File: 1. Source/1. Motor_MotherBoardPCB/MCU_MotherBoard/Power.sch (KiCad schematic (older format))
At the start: 3 parts, among them J10 Connector_JST_01x02, J9 Connector_JST_01x02, U20 LM7805CT

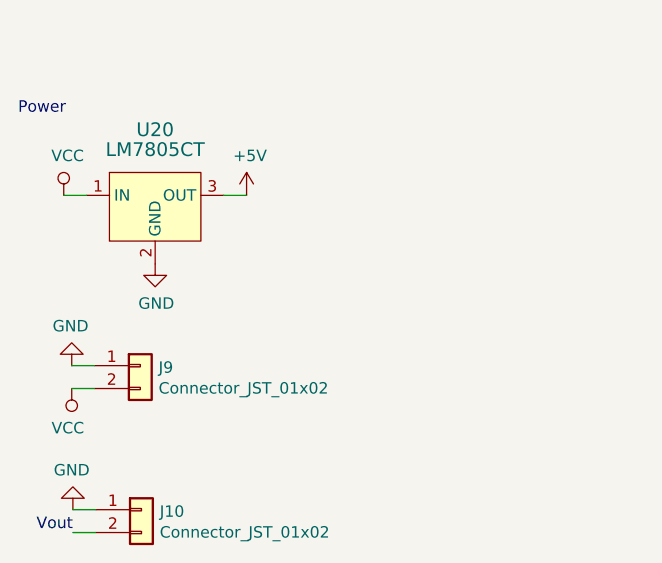
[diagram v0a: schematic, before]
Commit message: Schematic finished
- change cap`s footprint to smd type
- artwork should be done.
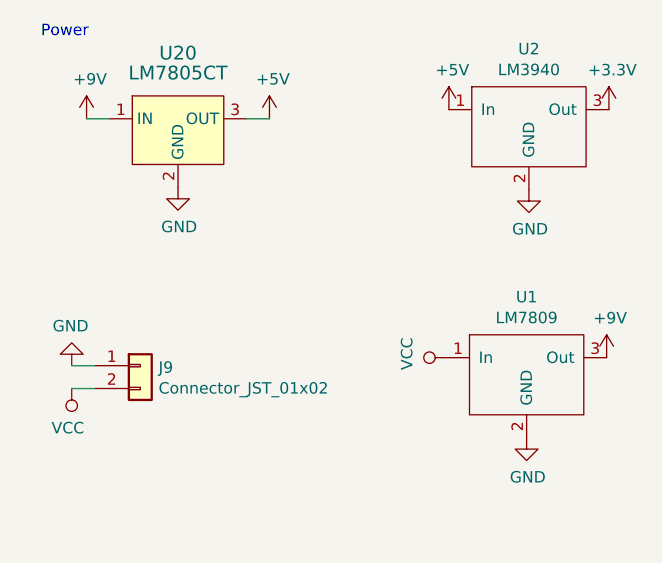
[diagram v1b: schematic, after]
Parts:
- removed J10: Connector_JST_01x02, Connectors_JST:JST_XH_S02B-XH-A_02x2.50mm_Angled, symbol BC_Connectors:Connector_JST_01x02
- added U1: LM7809, digikey-footprints:TO-220-3, symbol BC_IC_components:LM7809
- added U2: LM3940, digikey-footprints:TO-220-3, symbol BC_IC_components:LM3940
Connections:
- net +5V: now also U2.1 (In)
- net GND: now also U1.2 (GND), U2.2 (GND)
- net VCC: now also U1.1 (In); no longer U20.1 (IN)
- new net +3V3: U2.3 (Out)
- new net +9V: U1.3 (Out), U20.1 (IN)
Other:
- moved on the sheet: U20
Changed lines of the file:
@@
 Comment4 ""
 $EndDescr
-$Comp
-L dk_PMIC-Voltage-Regulators-Linear:LM7805CT_Obsolete U?
-U 1 1 6389FF7E
-P 3430 2550
-AR Path="/6387462E/6389FF7E" Ref="U?"  Part="1"
-AR Path="/6386EE9C/6389FF7E" Ref="U20"  Part="1"
-F 0 "U20" H 3430 2837 60  0000 C CNN
-F 1 "LM7805CT" H 3430 2750 60  0000 C CNN
-F 2 "digikey-footprints:TO-220-3" H 3630 2750 60  0001 L CNN
-F 3 "https://media.digikey.com/pdf/Data%20Sheets/ON%20Semiconductor%20PDFs/MC7800(A,AE),NCV7800.pdf" H 3630 2850 60  0001 L CNN
-F 4 "LM7805CT-ND" H 3630 2950 60  0001 L CNN "Digi-Key_PN"
-F 5 "LM7805CT" H 3630 3050 60  0001 L CNN "MPN"
-F 6 "Integrated Circuits (ICs)" H 3630 3150 60  0001 L CNN "Category"
-F 7 "PMIC - Voltage Regulators - Linear" H 3630 3250 60  0001 L CNN "Family"
-F 8 "https://media.digikey.com/pdf/Data%20Sheets/ON%20Semiconductor%20PDFs/MC7800(A,AE),NCV7800.pdf" H 3630 3350 60  0001 L CNN "DK_Datasheet_Link"
-F 9 "/product-detail/en/on-semiconductor/LM7805CT/LM7805CT-ND/458698" H 3630 3450 60  0001 L CNN "DK_Detail_Page"
-F 10 "IC REG LINEAR 5V 1A TO220AB" H 3630 3550 60  0001 L CNN "Description"
-F 11 "ON Semiconductor" H 3630 3650 60  0001 L CNN "Manufacturer"
-F 12 "Obsolete NonStock" H 3630 3750 60  0001 L CNN "Status"
-	1    3430 2550
-	1    0    0    -1
-$EndComp
-$Comp
-L power:VCC #PWR?
-U 1 1 6389FF84
-P 3030 2550
-AR Path="/6387462E/6389FF84" Ref="#PWR?"  Part="1"
-AR Path="/6386EE9C/6389FF84" Ref="#PWR021"  Part="1"
-F 0 "#PWR021" H 3030 2400 50  0001 C CNN
-F 1 "VCC" H 3047 2723 50  0000 C CNN
-F 2 "" H 3030 2550 50  0001 C CNN
-F 3 "" H 3030 2550 50  0001 C CNN
-	1    3030 2550
-	1    0    0    -1
-$EndComp
 Wire Wire Line
-	3030 2550 3130 2550
+	3130 2215 3230 2215
 Wire Wire Line
-	3730 2550 3830 2550
+	3830 2215 3930 2215
 $Comp
 L power:GND #PWR?
 U 1 1 6389FF8C
-P 3430 2850
+P 3530 2515
 AR Path="/6387462E/6389FF8C" Ref="#PWR?"  Part="1"
 AR Path="/6386EE9C/6389FF8C" Ref="#PWR025"  Part="1"
-F 0 "#PWR025" H 3430 2600 50  0001 C CNN
-F 1 "GND" H 3435 2677 50  0000 C CNN
-F 2 "" H 3430 2850 50  0001 C CNN
-F 3 "" H 3430 2850 50  0001 C CNN
-	1    3430 2850
+F 0 "#PWR025" H 3530 2265 50  0001 C CNN
+F 1 "GND" H 3535 2342 50  0000 C CNN
+F 2 "" H 3530 2515 50  0001 C CNN
+F 3 "" H 3530 2515 50  0001 C CNN
+	1    3530 2515
 	1    0    0    -1
 $EndComp
@@
 L power:+5V #PWR?
 U 1 1 6389FFA6
-P 3830 2550
+P 3930 2215
 AR Path="/6387462E/6389FFA6" Ref="#PWR?"  Part="1"
 AR Path="/6386EE9C/6389FFA6" Ref="#PWR026"  Part="1"
-F 0 "#PWR026" H 3830 2400 50  0001 C CNN
-F 1 "+5V" H 3845 2723 50  0000 C CNN
-F 2 "" H 3830 2550 50  0001 C CNN
-F 3 "" H 3830 2550 50  0001 C CNN
-	1    3830 2550
+F 0 "#PWR026" H 3930 2065 50  0001 C CNN
+F 1 "+5V" H 3945 2388 50  0000 C CNN
+F 2 "" H 3930 2215 50  0001 C CNN
+F 3 "" H 3930 2215 50  0001 C CNN
+	1    3930 2215
 	1    0    0    -1
 $EndComp
-Text Notes 2830 2200 0    50   ~ 0
+Text Notes 2930 1865 0    50   ~ 0
 Power
-Text Label 3070 4025 2    50   ~ 0
-Vout
-Wire Wire Line
-	3170 3925 3070 3925
-Wire Wire Line
-	3070 4025 3170 4025
-$Comp
-L power:GND #PWR024
-U 1 1 6389FFB3
-P 3070 3925
-F 0 "#PWR024" H 3070 3675 50  0001 C CNN
-F 1 "GND" H 3075 3752 50  0000 C CNN
-F 2 "" H 3070 3925 50  0001 C CNN
-F 3 "" H 3070 3925 50  0001 C CNN
-	1    3070 3925
-	-1   0    0    1
-$EndComp
-$Comp
-L BC_Connectors:Connector_JST_01x02 J10
-U 1 1 6389FFAD
-P 3370 3925
-F 0 "J10" H 3450 3917 50  0000 L CNN
-F 1 "Connector_JST_01x02" H 3450 3826 50  0000 L CNN
-F 2 "Connectors_JST:JST_XH_S02B-XH-A_02x2.50mm_Angled" H 3370 3925 50  0001 C CNN
-F 3 "" H 3370 3925 50  0001 C CNN
-	1    3370 3925
-	1    0    0    -1
-$EndComp
 Wire Wire Line
 	3165 3295 3065 3295
@@
 	1    0    0    -1
 $EndComp
+$Comp
+L BC_IC_components:LM3940 U2
+U 1 1 6386AA1C
+P 5065 2075
+F 0 "U2" H 5065 2240 50  0000 C CNN
+F 1 "LM3940" H 5065 2149 50  0000 C CNN
+F 2 "digikey-footprints:TO-220-3" H 5065 2075 50  0001 C CNN
+F 3 "" H 5065 2075 50  0001 C CNN
+	1    5065 2075
+	1    0    0    -1
+$EndComp
+$Comp
+L power:+5V #PWR?
+U 1 1 6386B945
+P 4715 2175
+AR Path="/6387462E/6386B945" Ref="#PWR?"  Part="1"
+AR Path="/6386EE9C/6386B945" Ref="#PWR033"  Part="1"
+F 0 "#PWR033" H 4715 2025 50  0001 C CNN
+F 1 "+5V" H 4730 2348 50  0000 C CNN
+F 2 "" H 4715 2175 50  0001 C CNN
+F 3 "" H 4715 2175 50  0001 C CNN
+	1    4715 2175
+	1    0    0    -1
+$EndComp
+$Comp
+L power:GND #PWR?
+U 1 1 6386D2CB
+P 5065 2525
+AR Path="/6387462E/6386D2CB" Ref="#PWR?"  Part="1"
+AR Path="/6386EE9C/6386D2CB" Ref="#PWR041"  Part="1"
+F 0 "#PWR041" H 5065 2275 50  0001 C CNN
+F 1 "GND" H 5070 2352 50  0000 C CNN
+F 2 "" H 5065 2525 50  0001 C CNN
+F 3 "" H 5065 2525 50  0001 C CNN
+	1    5065 2525
+	1    0    0    -1
+$EndComp
+$Comp
+L power:+3.3V #PWR046
+U 1 1 6386D97A
+P 5415 2175
+F 0 "#PWR046" H 5415 2025 50  0001 C CNN
+F 1 "+3.3V" H 5430 2348 50  0000 C CNN
+F 2 "" H 5415 2175 50  0001 C CNN
+F 3 "" H 5415 2175 50  0001 C CNN
+	1    5415 2175
+	1    0    0    -1
+$EndComp
+$Comp
+L power:+9V #PWR021
+U 1 1 6389536F
+P 3130 2215
+F 0 "#PWR021" H 3130 2065 50  0001 C CNN
+F 1 "+9V" H 3145 2388 50  0000 C CNN
+F 2 "" H 3130 2215 50  0001 C CNN
+F 3 "" H 3130 2215 50  0001 C CNN
+	1    3130 2215
+	1    0    0    -1
+$EndComp
+$Comp
+L BC_IC_components:LM7809 U1
+U 1 1 6389B080
+P 5055 3160
+F 0 "U1" H 5055 3325 50  0000 C CNN
+F 1 "LM7809" H 5055 3234 50  0000 C CNN
+F 2 "digikey-footprints:TO-220-3" H 5055 3160 50  0001 C CNN
+F 3 "" H 5055 3160 50  0001 C CNN
+	1    5055 3160
+	1    0    0    -1
+$EndComp
+$Comp
+L power:GND #PWR?
+U 1 1 6389B64A
+P 5055 3610
+AR Path="/6387462E/6389B64A" Ref="#PWR?"  Part="1"
+AR Path="/6386EE9C/6389B64A" Ref="#PWR034"  Part="1"
+F 0 "#PWR034" H 5055 3360 50  0001 C CNN
+F 1 "GND" H 5060 3437 50  0000 C CNN
+F 2 "" H 5055 3610 50  0001 C CNN
+F 3 "" H 5055 3610 50  0001 C CNN
+	1    5055 3610
+	1    0    0    -1
+$EndComp
+$Comp
+L power:+9V #PWR044
+U 1 1 6389BE13
+P 5405 3260
+F 0 "#PWR044" H 5405 3110 50  0001 C CNN
+F 1 "+9V" H 5420 3433 50  0000 C CNN
+F 2 "" H 5405 3260 50  0001 C CNN
+F 3 "" H 5405 3260 50  0001 C CNN
+	1    5405 3260
+	1    0    0    -1
+$EndComp
+$Comp
+L power:VCC #PWR030
+U 1 1 6389C757
+P 4705 3260
+F 0 "#PWR030" H 4705 3110 50  0001 C CNN
+F 1 "VCC" H 4722 3433 50  0000 C CNN
+F 2 "" H 4705 3260 50  0001 C CNN
+F 3 "" H 4705 3260 50  0001 C CNN
+	1    4705 3260
+	0    -1   -1   0
+$EndComp
+$Comp
+L dk_PMIC-Voltage-Regulators-Linear:LM7805CT_Obsolete U?
+U 1 1 6389FF7E
+P 3530 2215
+AR Path="/6387462E/6389FF7E" Ref="U?"  Part="1"
+AR Path="/6386EE9C/6389FF7E" Ref="U20"  Part="1"
+F 0 "U20" H 3530 2502 60  0000 C CNN
+F 1 "LM7805CT" H 3530 2415 60  0000 C CNN
+F 2 "digikey-footprints:TO-220-3" H 3730 2415 60  0001 L CNN
+F 3 "https://media.digikey.com/pdf/Data%20Sheets/ON%20Semiconductor%20PDFs/MC7800(A,AE),NCV7800.pdf" H 3730 2515 60  0001 L CNN
+F 4 "LM7805CT-ND" H 3730 2615 60  0001 L CNN "Digi-Key_PN"
+F 5 "LM7805CT" H 3730 2715 60  0001 L CNN "MPN"
+F 6 "Integrated Circuits (ICs)" H 3730 2815 60  0001 L CNN "Category"
+F 7 "PMIC - Voltage Regulators - Linear" H 3730 2915 60  0001 L CNN "Family"
+F 8 "https://media.digikey.com/pdf/Data%20Sheets/ON%20Semiconductor%20PDFs/MC7800(A,AE),NCV7800.pdf" H 3730 3015 60  0001 L CNN "DK_Datasheet_Link"
+F 9 "/product-detail/en/on-semiconductor/LM7805CT/LM7805CT-ND/458698" H 3730 3115 60  0001 L CNN "DK_Detail_Page"
+F 10 "IC REG LINEAR 5V 1A TO220AB" H 3730 3215 60  0001 L CNN "Description"
+F 11 "ON Semiconductor" H 3730 3315 60  0001 L CNN "Manufacturer"
+F 12 "Obsolete NonStock" H 3730 3415 60  0001 L CNN "Status"
+	1    3530 2215
+	1    0    0    -1
+$EndComp
